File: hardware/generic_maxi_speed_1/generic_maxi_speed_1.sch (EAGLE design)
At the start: 34 parts, among them IC1 MEGA48/88/168-PU, IC2 RFM12, IC3 LP2950Z, Q1 20MHz

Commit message: add generic maxi speed layout
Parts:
- removed H1, H2, H3: MOUNT-HOLE2.8, holes:MOUNT-HOLE2.8
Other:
- note added: "Date: 30.04.2013"
- note removed: "Date: 28.04.2013"
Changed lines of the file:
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@@
 <part name="R7" library="rcl" deviceset="R-EU_" device="0207/7" value="3k3"/>
 <part name="C6" library="rcl" deviceset="CPOL-EU" device="E1.8-4" value="10µ"/>
-<part name="H1" library="holes" deviceset="MOUNT-HOLE" device="2.8"/>
-<part name="H2" library="holes" deviceset="MOUNT-HOLE" device="2.8"/>
-<part name="H3" library="holes" deviceset="MOUNT-HOLE" device="2.8"/>
 <part name="JP6" library="pinhead" deviceset="PINHD-1X1" device="" value="ANT"/>
 <part name="JP7" library="pinhead" deviceset="PINHD-1X1" device="" value="ANT"/>
@@
 <frame x1="-60.96" y1="-58.42" x2="172.72" y2="93.98" columns="8" rows="5" layer="97"/>
 <text x="66.04" y="-40.64" size="3.81" layer="97">Open Home Control Generic Maxi Speed 1</text>
-<text x="121.92" y="-45.72" size="2.1844" layer="97">Date: 28.04.2013</text>
+<text x="121.92" y="-45.72" size="2.1844" layer="97">Date: 30.04.2013</text>
 <text x="66.04" y="-45.72" size="2.1844" layer="97">Rev 1.0</text>
 <text x="66.04" y="-50.8" size="2.1844" layer="97">Copyright (c) Uwe Freese, www.open-home-control.com</text>
@@
 <instance part="R7" gate="G$1" x="111.76" y="0"/>
 <instance part="C6" gate="G$1" x="-40.64" y="17.78" rot="R270"/>
-<instance part="H1" gate="G$1" x="132.08" y="-25.4"/>
-<instance part="H2" gate="G$1" x="132.08" y="-20.32"/>
-<instance part="H3" gate="G$1" x="132.08" y="-15.24"/>
 <instance part="JP6" gate="G$1" x="58.42" y="38.1"/>
 <instance part="JP7" gate="G$1" x="58.42" y="35.56"/>

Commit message: Moved capacitor near to RFM12. Added zener diodes instead of resistors. Avoid one bridge connection.
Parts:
- removed R7, R8, R9: 3k3, rcl:R-EU_0207/7
- added D2, D3, D4: 3.3V, diode:ZENER-DIODEZD-5
- JP12: value (none) -> FEATURE
- R4, R5, R6: value 1k8 -> 1k
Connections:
- net GND: now also D2.A, D3.A, D4.A; no longer R7.2, R8.2, R9.2
- net N$16: now also D3.C; no longer R8.1
- net N$27: now also D2.C; no longer R7.1
- net N$5: now also D4.C; no longer R9.1
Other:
- note added: "Date: 01.05.2013"
- note added: "Rev x.x"
- note removed: "Date: 30.04.2013"
- note removed: "Rev 1.0"
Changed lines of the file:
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@@
 <part name="+3V3" library="supply1" deviceset="+3V3" device=""/>
 <part name="P+2" library="supply1" deviceset="+5V" device=""/>
-<part name="R5" library="rcl" deviceset="R-EU_" device="0207/7" value="1k8"/>
-<part name="R8" library="rcl" deviceset="R-EU_" device="0207/7" value="3k3"/>
-<part name="R6" library="rcl" deviceset="R-EU_" device="0207/7" value="1k8"/>
-<part name="R9" library="rcl" deviceset="R-EU_" device="0207/7" value="3k3"/>
-<part name="R4" library="rcl" deviceset="R-EU_" device="0207/7" value="1k8"/>
-<part name="R7" library="rcl" deviceset="R-EU_" device="0207/7" value="3k3"/>
+<part name="R5" library="rcl" deviceset="R-EU_" device="0207/7" value="1k"/>
+<part name="R6" library="rcl" deviceset="R-EU_" device="0207/7" value="1k"/>
+<part name="R4" library="rcl" deviceset="R-EU_" device="0207/7" value="1k"/>
 <part name="C6" library="rcl" deviceset="CPOL-EU" device="E1.8-4" value="10µ"/>
 <part name="JP6" library="pinhead" deviceset="PINHD-1X1" device="" value="ANT"/>
@@
 <part name="JP9" library="pinhead" deviceset="PINHD-1X1" device="" value="ANT"/>
 <part name="JP10" library="pinhead" deviceset="PINHD-1X1" device="" value="ANT"/>
-<part name="JP12" library="pinhead" deviceset="PINHD-1X5" device=""/>
+<part name="JP12" library="pinhead" deviceset="PINHD-1X5" device="" value="FEATURE"/>
+<part name="D2" library="diode" deviceset="ZENER-DIODE" device="ZD-5" value="3.3V"/>
+<part name="D3" library="diode" deviceset="ZENER-DIODE" device="ZD-5" value="3.3V"/>
+<part name="D4" library="diode" deviceset="ZENER-DIODE" device="ZD-5" value="3.3V"/>
 </parts>
 <sheets>
@@
 <frame x1="-60.96" y1="-58.42" x2="172.72" y2="93.98" columns="8" rows="5" layer="97"/>
 <text x="66.04" y="-40.64" size="3.81" layer="97">Open Home Control Generic Maxi Speed 1</text>
-<text x="121.92" y="-45.72" size="2.1844" layer="97">Date: 30.04.2013</text>
-<text x="66.04" y="-45.72" size="2.1844" layer="97">Rev 1.0</text>
+<text x="121.92" y="-45.72" size="2.1844" layer="97">Date: 01.05.2013</text>
+<text x="66.04" y="-45.72" size="2.1844" layer="97">Rev x.x</text>
 <text x="66.04" y="-50.8" size="2.1844" layer="97">Copyright (c) Uwe Freese, www.open-home-control.com</text>
 </plain>
@@
 <instance part="P+2" gate="1" x="73.66" y="78.74" rot="R270"/>
 <instance part="R5" gate="G$1" x="63.5" y="-5.08"/>
-<instance part="R8" gate="G$1" x="101.6" y="-5.08"/>
 <instance part="R6" gate="G$1" x="73.66" y="-10.16"/>
-<instance part="R9" gate="G$1" x="96.52" y="-10.16"/>
 <instance part="R4" gate="G$1" x="58.42" y="0"/>
-<instance part="R7" gate="G$1" x="111.76" y="0"/>
 <instance part="C6" gate="G$1" x="-40.64" y="17.78" rot="R270"/>
 <instance part="JP6" gate="G$1" x="58.42" y="38.1"/>
@@
 <instance part="JP10" gate="G$1" x="58.42" y="27.94"/>
 <instance part="JP12" gate="A" x="58.42" y="53.34"/>
+<instance part="D2" gate="G$1" x="114.3" y="0" rot="R180"/>
+<instance part="D3" gate="G$1" x="104.14" y="-5.08" rot="R180"/>
+<instance part="D4" gate="G$1" x="99.06" y="-10.16" rot="R180"/>
 </instances>
 <busses>
@@
 <junction x="137.16" y="55.88"/>
 <wire x1="147.32" y1="55.88" x2="152.4" y2="55.88" width="0.1524" layer="91"/>
-<pinref part="R8" gate="G$1" pin="2"/>
 <wire x1="106.68" y1="-5.08" x2="119.38" y2="-5.08" width="0.1524" layer="91"/>
 <junction x="119.38" y="-5.08"/>
-<pinref part="R9" gate="G$1" pin="2"/>
 <wire x1="101.6" y1="-10.16" x2="119.38" y2="-10.16" width="0.1524" layer="91"/>
 <junction x="119.38" y="-10.16"/>
-<pinref part="R7" gate="G$1" pin="2"/>
 <wire x1="116.84" y1="0" x2="119.38" y2="0" width="0.1524" layer="91"/>
 <junction x="119.38" y="0"/>
@@
 <wire x1="127" y1="53.34" x2="127" y2="55.88" width="0.1524" layer="91"/>
 <junction x="127" y="55.88"/>
+<pinref part="D2" gate="G$1" pin="A"/>
+<pinref part="D3" gate="G$1" pin="A"/>
+<pinref part="D4" gate="G$1" pin="A"/>
 </segment>
 <segment>
@@
 <wire x1="83.82" y1="27.94" x2="83.82" y2="7.62" width="0.1524" layer="91"/>
 <pinref part="R6" gate="G$1" pin="2"/>
-<pinref part="R9" gate="G$1" pin="1"/>
 <wire x1="78.74" y1="-10.16" x2="81.28" y2="-10.16" width="0.1524" layer="91"/>
 <wire x1="81.28" y1="-10.16" x2="91.44" y2="-10.16" width="0.1524" layer="91"/>
@@
 <wire x1="81.28" y1="7.62" x2="81.28" y2="-10.16" width="0.1524" layer="91"/>
 <junction x="81.28" y="-10.16"/>
+<pinref part="D4" gate="G$1" pin="C"/>
+<wire x1="91.44" y1="-10.16" x2="96.52" y2="-10.16" width="0.1524" layer="91"/>
 </segment>
 </net>
@@
 <wire x1="78.74" y1="12.7" x2="78.74" y2="-2.54" width="0.1524" layer="91"/>
 <pinref part="R5" gate="G$1" pin="2"/>
-<pinref part="R8" gate="G$1" pin="1"/>
 <wire x1="68.58" y1="-5.08" x2="78.74" y2="-5.08" width="0.1524" layer="91"/>
 <wire x1="78.74" y1="-5.08" x2="96.52" y2="-5.08" width="0.1524" layer="91"/>
 <wire x1="78.74" y1="-2.54" x2="78.74" y2="-5.08" width="0.1524" layer="91"/>
 <junction x="78.74" y="-5.08"/>
+<pinref part="D3" gate="G$1" pin="C"/>
+<wire x1="96.52" y1="-5.08" x2="101.6" y2="-5.08" width="0.1524" layer="91"/>
 </segment>
 </net>
@@
 <segment>
 <pinref part="R4" gate="G$1" pin="2"/>
-<pinref part="R7" gate="G$1" pin="1"/>
 <wire x1="63.5" y1="0" x2="106.68" y2="0" width="0.1524" layer="91"/>
 <pinref part="IC2" gate="G$1" pin="NSEL"/>
@@
 <wire x1="106.68" y1="7.62" x2="106.68" y2="27.94" width="0.1524" layer="91"/>
 <wire x1="106.68" y1="0" x2="106.68" y2="7.62" width="0.1524" layer="91"/>
+<junction x="106.68" y="7.62"/>
+<pinref part="D2" gate="G$1" pin="C"/>
+<wire x1="106.68" y1="0" x2="111.76" y2="0" width="0.1524" layer="91"/>
 <junction x="106.68" y="0"/>
-<junction x="106.68" y="7.62"/>
-</segment>
-</net>
+</segment>
+</net>

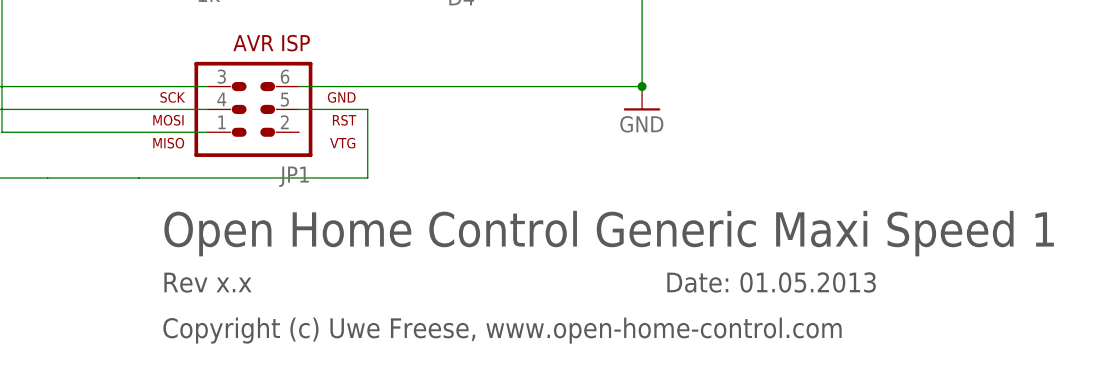
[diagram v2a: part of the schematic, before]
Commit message: Rev 1.0 finished, circuit working. Add mask and placing picture.
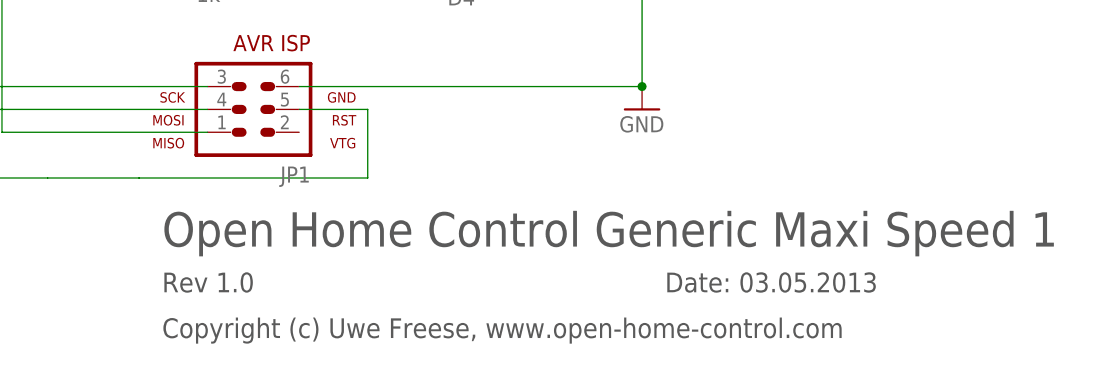
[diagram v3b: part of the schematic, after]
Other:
- note added: "Date: 03.05.2013"
- note added: "Rev 1.0"
- note removed: "Date: 01.05.2013"
- note removed: "Rev x.x"
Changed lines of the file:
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@@
 <frame x1="-60.96" y1="-58.42" x2="172.72" y2="93.98" columns="8" rows="5" layer="97"/>
 <text x="66.04" y="-40.64" size="3.81" layer="97">Open Home Control Generic Maxi Speed 1</text>
-<text x="121.92" y="-45.72" size="2.1844" layer="97">Date: 01.05.2013</text>
-<text x="66.04" y="-45.72" size="2.1844" layer="97">Rev x.x</text>
+<text x="121.92" y="-45.72" size="2.1844" layer="97">Date: 03.05.2013</text>
+<text x="66.04" y="-45.72" size="2.1844" layer="97">Rev 1.0</text>
 <text x="66.04" y="-50.8" size="2.1844" layer="97">Copyright (c) Uwe Freese, www.open-home-control.com</text>
 </plain>

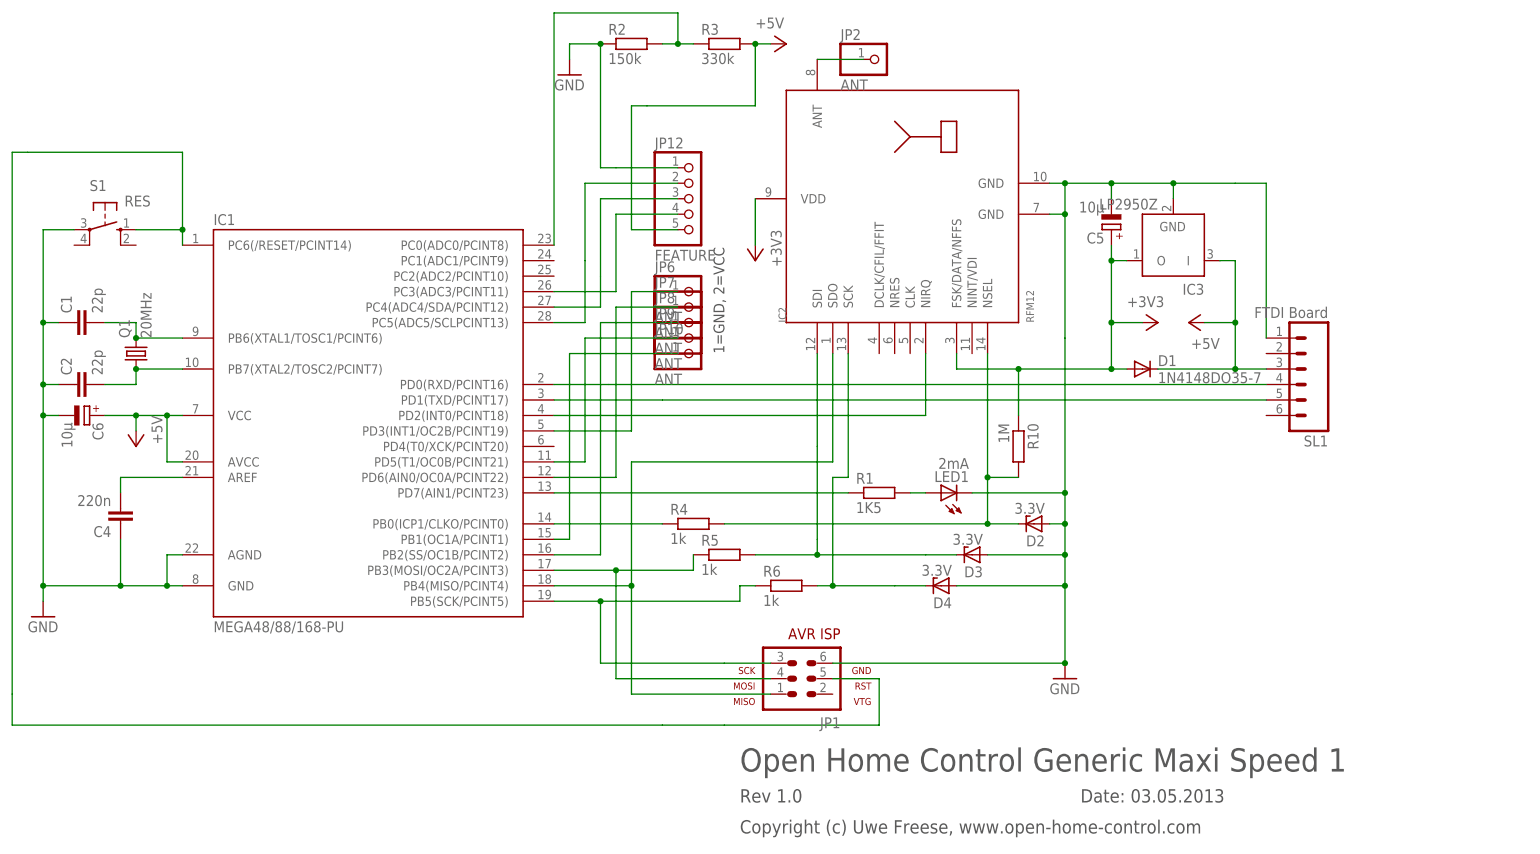
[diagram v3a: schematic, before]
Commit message: optimized label positions. Rename ATMega model in label.
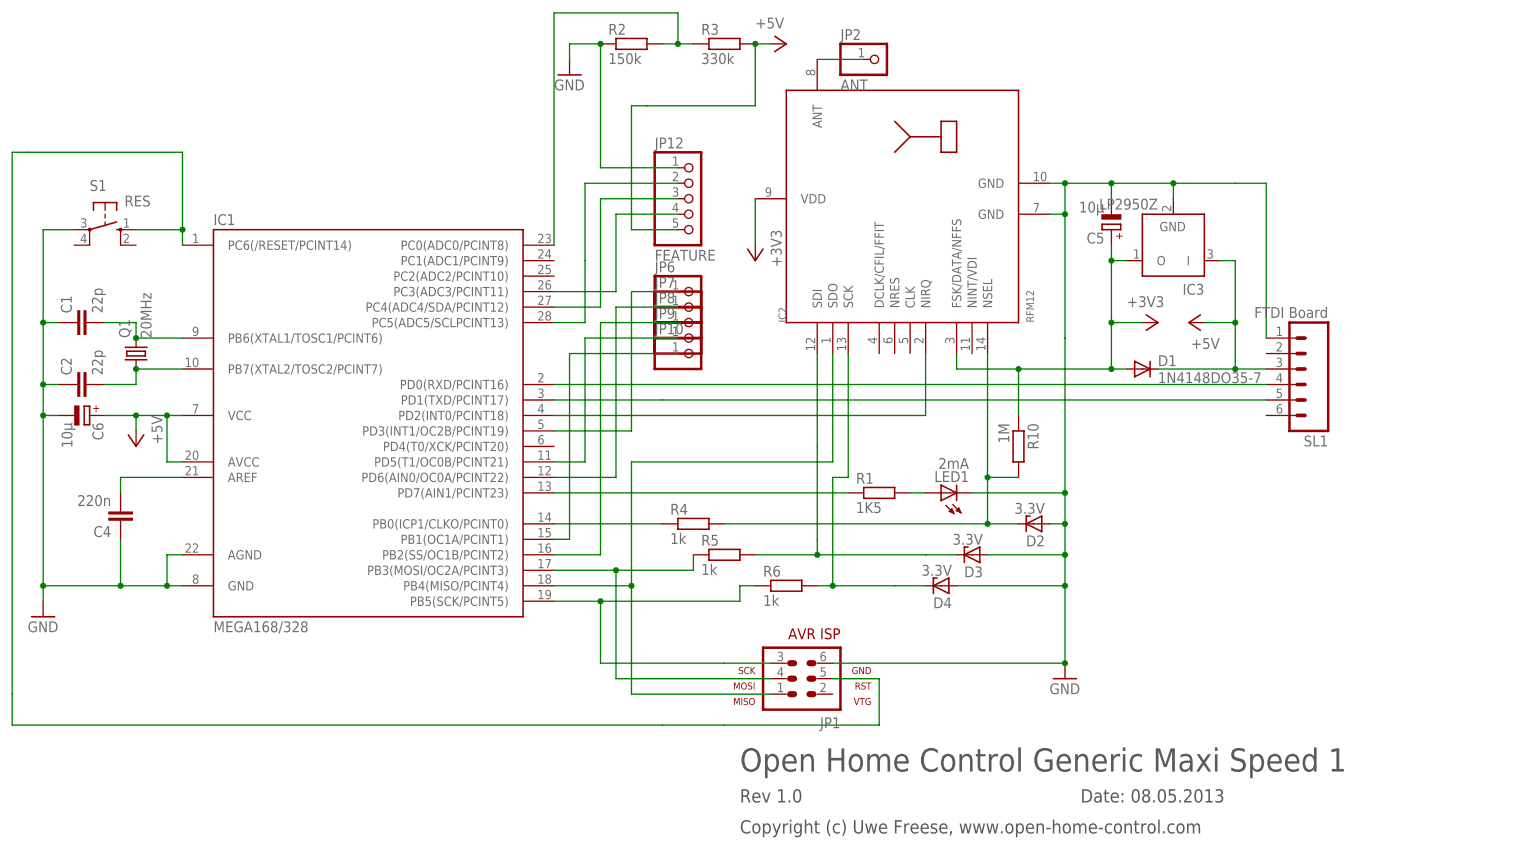
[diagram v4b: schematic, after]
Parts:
- IC1: value MEGA48/88/168-PU -> MEGA168/328
- JP10, JP6, JP7, JP8, JP9: value ANT -> (none)
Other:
- note added: "Date: 08.05.2013"
- note removed: "1=GND, 2=VCC"
- note removed: "Date: 03.05.2013"
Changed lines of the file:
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@@
 <?xml version="1.0" encoding="utf-8"?>
 <!DOCTYPE eagle SYSTEM "eagle.dtd">
-<eagle version="6.2">
+<eagle version="6.4">
 <drawing>
 <settings>
@@
 <part name="IC2" library="hopeRF" deviceset="RFM12" device=""/>
 <part name="LED1" library="led" deviceset="LED" device="3MM" value="2mA"/>
-<part name="IC1" library="avr-5-4.16" deviceset="MEGA48/88/168-PU" device=""/>
+<part name="IC1" library="avr-5-4.16" deviceset="MEGA48/88/168-PU" device="" value="MEGA168/328"/>
 <part name="JP1" library="avr-5-4.16" deviceset="AVR-ISP-6" device=""/>
 <part name="Q1" library="crystal" deviceset="CRYSTAL" device="HC49S" value="20MHz"/>
@@
 <part name="R4" library="rcl" deviceset="R-EU_" device="0207/7" value="1k"/>
 <part name="C6" library="rcl" deviceset="CPOL-EU" device="E1.8-4" value="10µ"/>
-<part name="JP6" library="pinhead" deviceset="PINHD-1X1" device="" value="ANT"/>
-<part name="JP7" library="pinhead" deviceset="PINHD-1X1" device="" value="ANT"/>
-<part name="JP8" library="pinhead" deviceset="PINHD-1X1" device="" value="ANT"/>
-<part name="JP9" library="pinhead" deviceset="PINHD-1X1" device="" value="ANT"/>
-<part name="JP10" library="pinhead" deviceset="PINHD-1X1" device="" value="ANT"/>
+<part name="JP6" library="pinhead" deviceset="PINHD-1X1" device=""/>
+<part name="JP7" library="pinhead" deviceset="PINHD-1X1" device=""/>
+<part name="JP8" library="pinhead" deviceset="PINHD-1X1" device=""/>
+<part name="JP9" library="pinhead" deviceset="PINHD-1X1" device=""/>
+<part name="JP10" library="pinhead" deviceset="PINHD-1X1" device=""/>
 <part name="JP12" library="pinhead" deviceset="PINHD-1X5" device="" value="FEATURE"/>
 <part name="D2" library="diode" deviceset="ZENER-DIODE" device="ZD-5" value="3.3V"/>
@@
 <sheet>
 <plain>
-<text x="63.5" y="27.94" size="1.778" layer="97" rot="R90">1=GND, 2=VCC</text>
 <frame x1="-60.96" y1="-58.42" x2="172.72" y2="93.98" columns="8" rows="5" layer="97"/>
 <text x="66.04" y="-40.64" size="3.81" layer="97">Open Home Control Generic Maxi Speed 1</text>
-<text x="121.92" y="-45.72" size="2.1844" layer="97">Date: 03.05.2013</text>
+<text x="121.92" y="-45.72" size="2.1844" layer="97">Date: 08.05.2013</text>
 <text x="66.04" y="-45.72" size="2.1844" layer="97">Rev 1.0</text>
 <text x="66.04" y="-50.8" size="2.1844" layer="97">Copyright (c) Uwe Freese, www.open-home-control.com</text>
